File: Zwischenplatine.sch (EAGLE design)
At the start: 9 parts

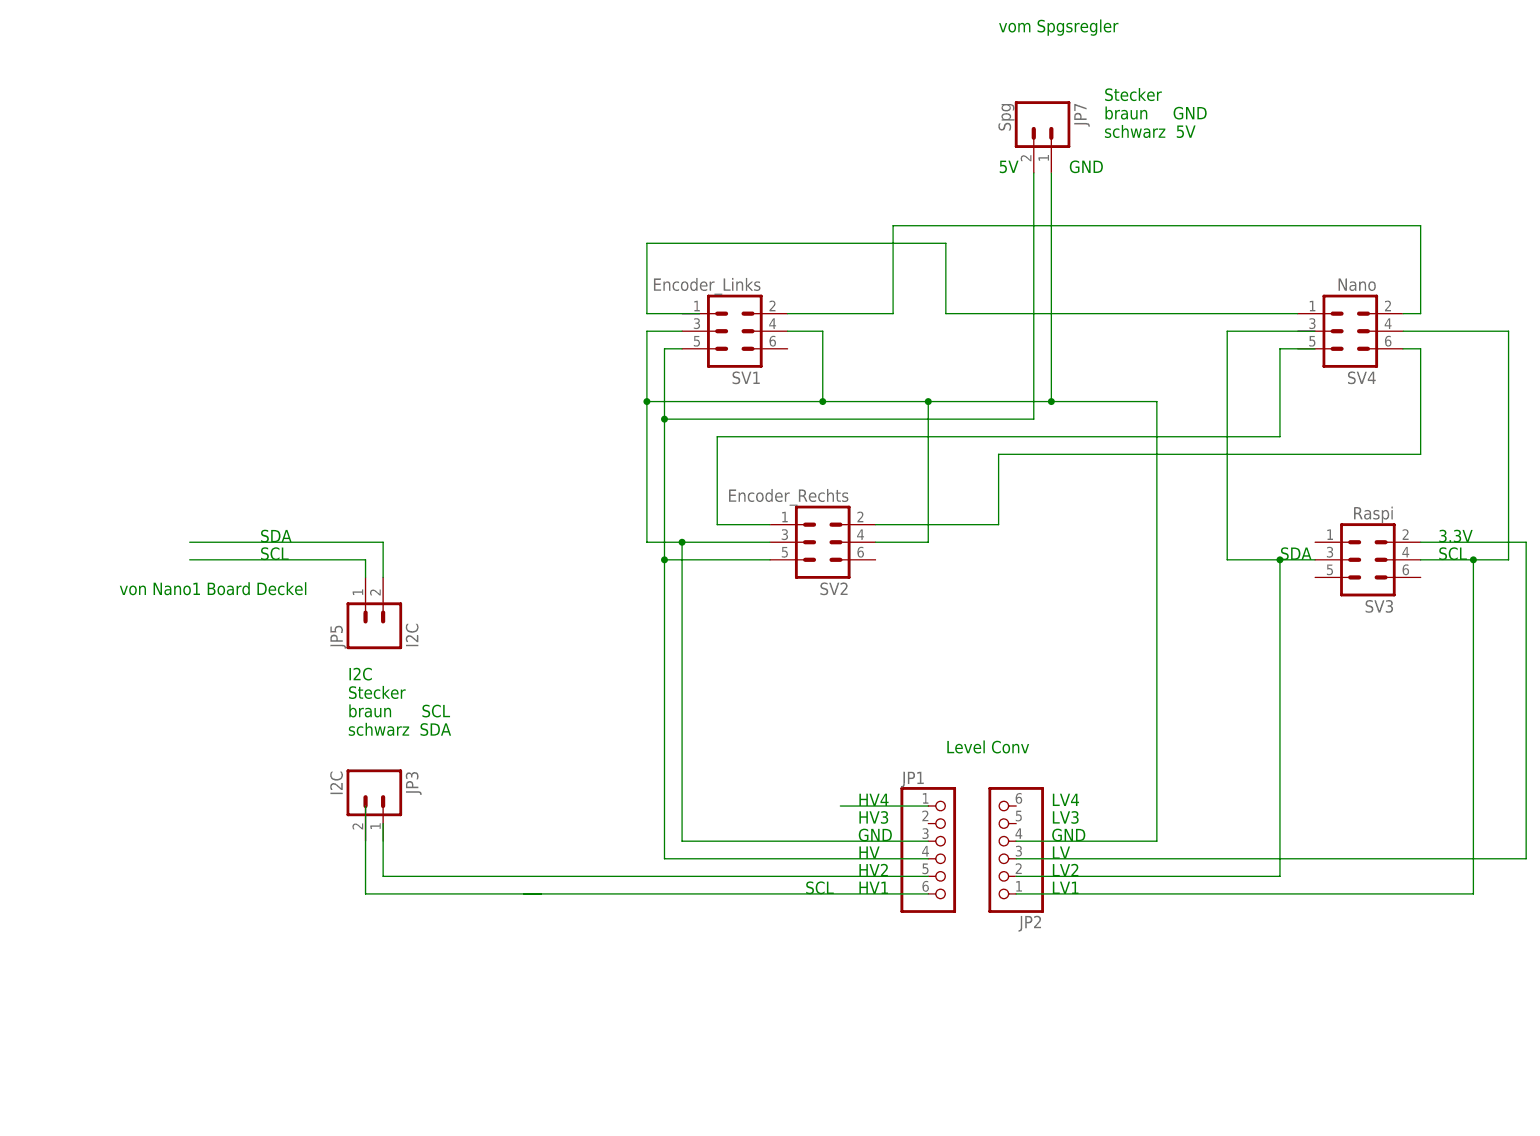
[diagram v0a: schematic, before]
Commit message: 
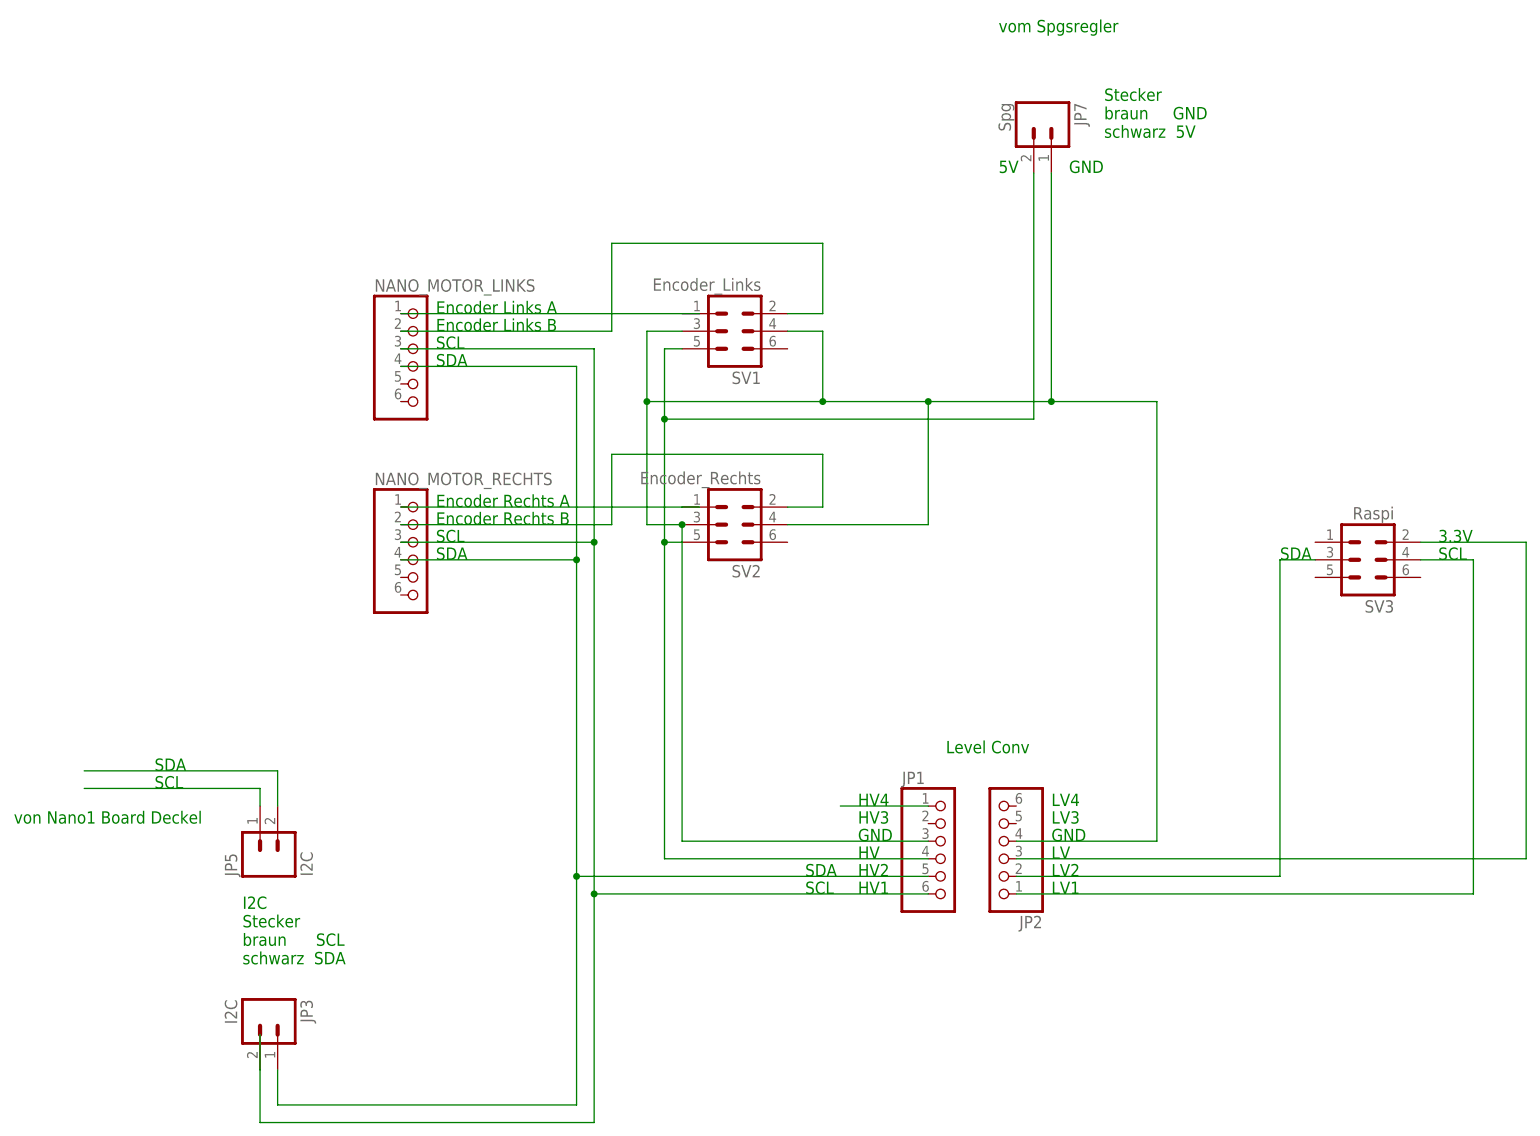
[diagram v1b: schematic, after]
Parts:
- removed SV4: Nano, con-ml:ML6
- added NANO_MOTOR_LINKS, NANO_MOTOR_RECHTS: (no value), adafruit:PINHD-1X6B
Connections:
- removed net N$15: JP1.6
- removed net N$4: JP1.5
- removed net PE4: SV1.2, SV4.2
- removed net PE5: SV2.2, SV4.6
- new net N$10: NANO_MOTOR_LINKS.2, SV1.2
- new net N$16: JP1.5, JP3.2, NANO_MOTOR_LINKS.4, NANO_MOTOR_RECHTS.4
- new net N$6: NANO_MOTOR_RECHTS.1, SV2.1
- new net N$8: NANO_MOTOR_LINKS.1
- net N$14: no longer SV4.4
- net N$7: now also NANO_MOTOR_RECHTS.2, SV2.2; no longer SV4.1
- net N$9: now also JP1.6, JP3.1, NANO_MOTOR_LINKS.3, NANO_MOTOR_RECHTS.3; no longer SV2.1
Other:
- note added: "Encoder Links A"
- note added: "Encoder Links B"
- note added: "Encoder Rechts A"
- note added: "Encoder Rechts B"
- moved on the sheet: JP3, JP5, SV2
